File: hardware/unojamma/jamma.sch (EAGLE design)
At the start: 3 parts

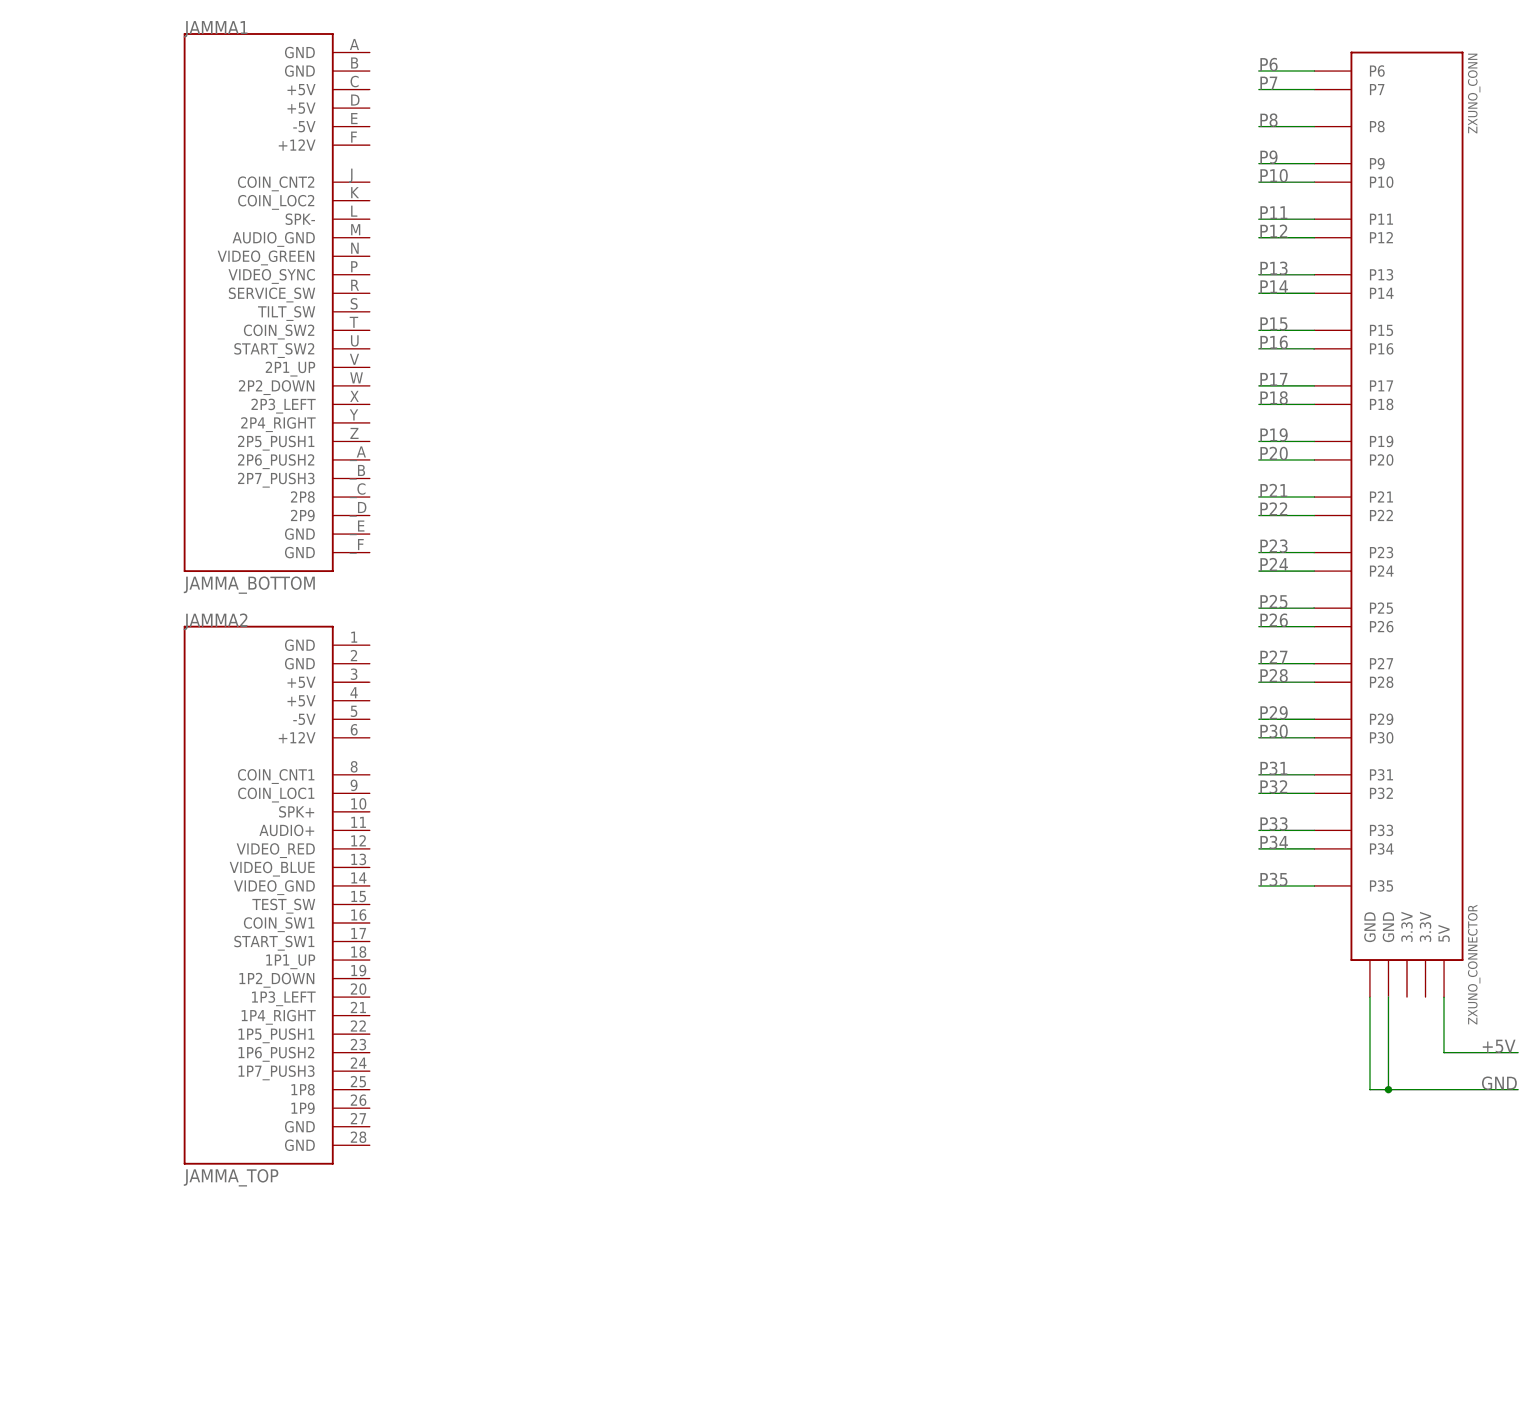
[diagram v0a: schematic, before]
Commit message: Añado conectores y separo placa para que quepa en 10x10cm
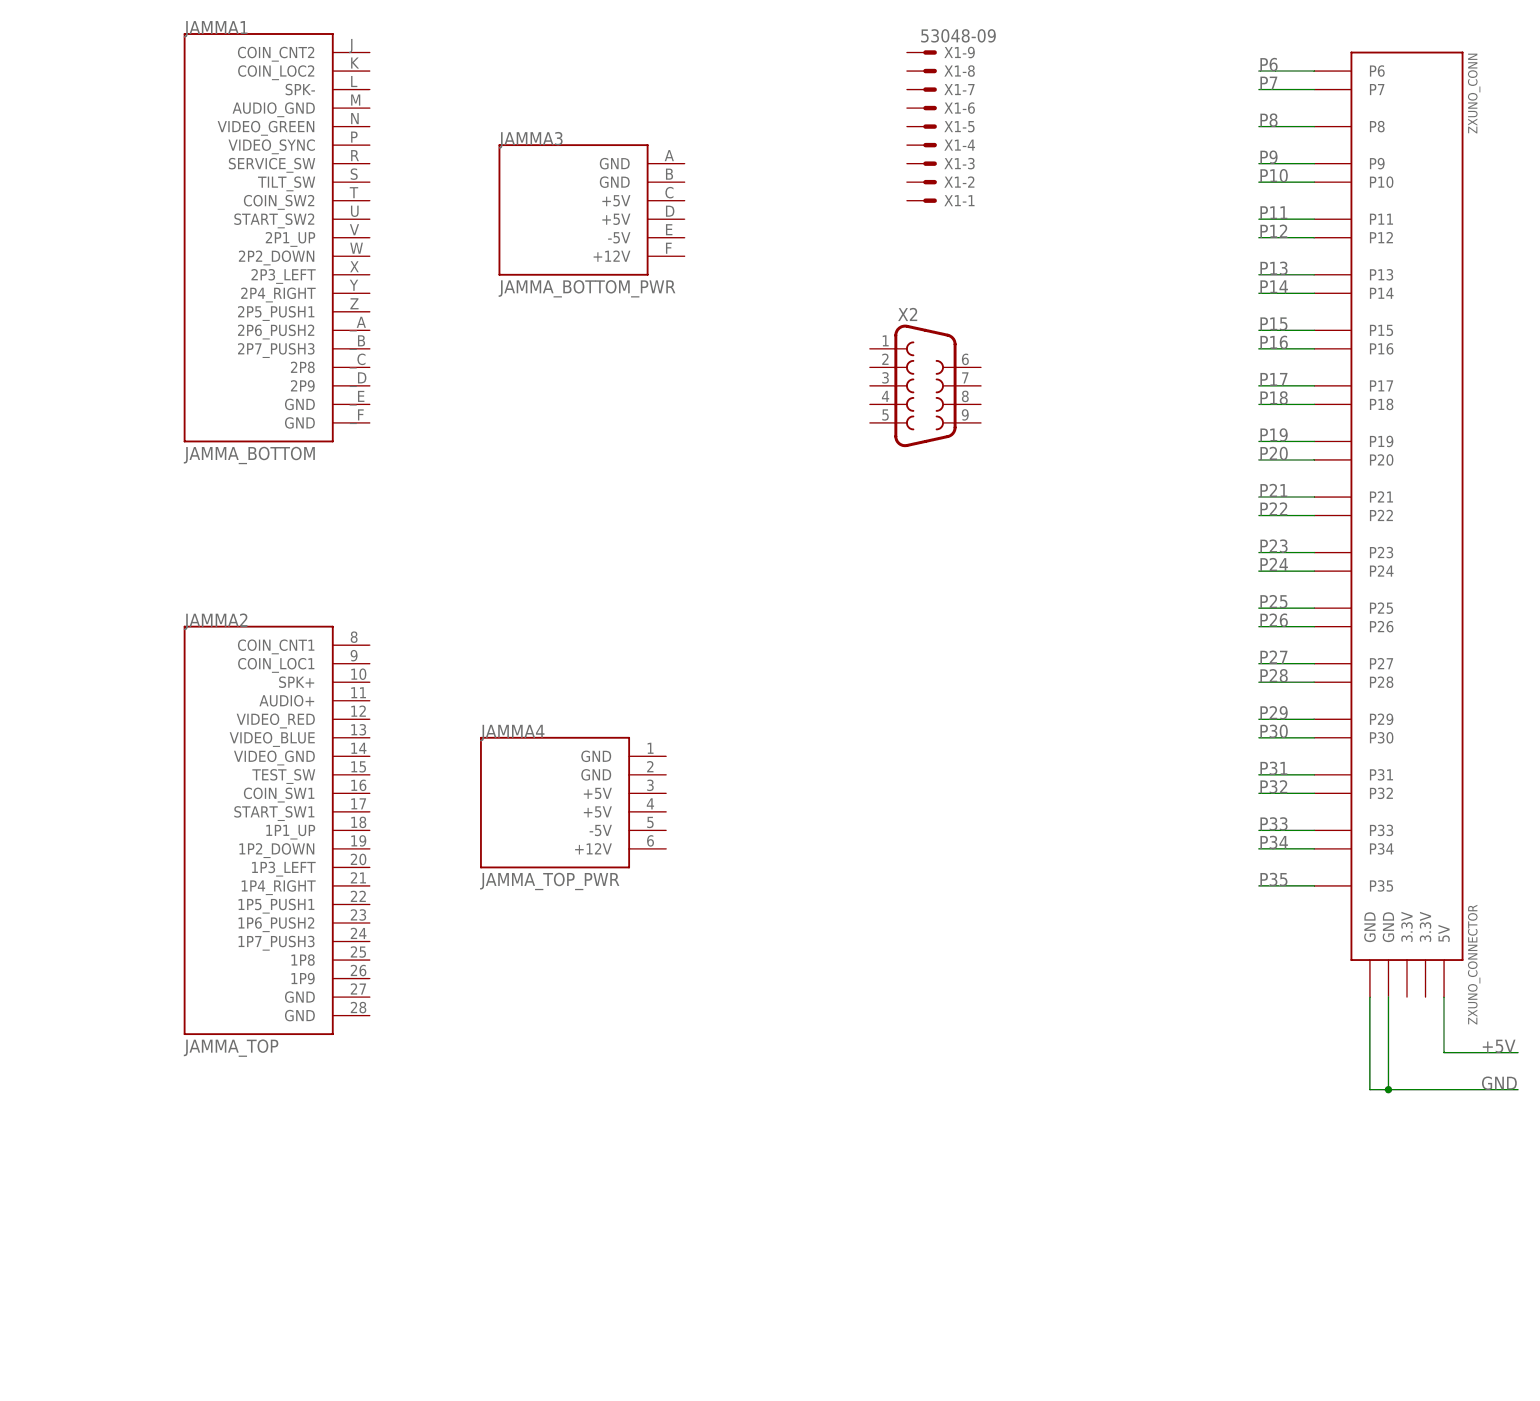
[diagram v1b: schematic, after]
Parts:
- added JAMMA3: JAMMA_BOTTOM_PWR, JAMMA_pwr:JAMMA_BOTTOM_PWR
- added JAMMA4: JAMMA_TOP_PWR, JAMMA_pwr:JAMMA_TOP_PWR
- added X1: 53048-09, con-molex:53048-09
- added X2: (no value), SparkFun-Connectors:DB9MALE
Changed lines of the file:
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@@
 <layer number="54" name="bGND_GNDA" color="7" fill="1" visible="no" active="no"/>
 <layer number="56" name="wert" color="7" fill="1" visible="no" active="no"/>
+<layer number="57" name="tCAD" color="7" fill="1" visible="no" active="no"/>
 <layer number="90" name="Modules" color="5" fill="1" visible="yes" active="yes"/>
 <layer number="91" name="Nets" color="2" fill="1" visible="yes" active="yes"/>
@@
 <layer number="97" name="Info" color="7" fill="1" visible="yes" active="yes"/>
 <layer number="98" name="Guide" color="6" fill="1" visible="yes" active="yes"/>
+<layer number="99" name="SpiceOrder" color="7" fill="1" visible="yes" active="yes"/>
 <layer number="100" name="Muster" color="7" fill="1" visible="yes" active="yes"/>
 <layer number="101" name="Patch_Top" color="7" fill="1" visible="yes" active="yes"/>
@@
 <layer number="111" name="LPC17xx" color="7" fill="1" visible="yes" active="yes"/>
 <layer number="112" name="tSilk" color="7" fill="1" visible="yes" active="yes"/>
+<layer number="113" name="IDFDebug" color="7" fill="1" visible="yes" active="yes"/>
 <layer number="116" name="Patch_BOT" color="7" fill="1" visible="yes" active="yes"/>
+<layer number="118" name="Rect_Pads" color="7" fill="1" visible="yes" active="yes"/>
 <layer number="121" name="_tsilk" color="7" fill="1" visible="yes" active="yes"/>
 <layer number="122" name="_bsilk" color="7" fill="1" visible="yes" active="yes"/>
@@
 <layer number="127" name="_tValues" color="7" fill="1" visible="yes" active="yes"/>
 <layer number="128" name="_bValues" color="7" fill="1" visible="yes" active="yes"/>
+<layer number="130" name="tSilk" color="7" fill="1" visible="yes" active="yes"/>
 <layer number="131" name="prix" color="7" fill="1" visible="yes" active="yes"/>
 <layer number="132" name="test" color="7" fill="1" visible="yes" active="yes"/>
+<layer number="133" name="Ports" color="7" fill="1" visible="yes" active="yes"/>
+<layer number="134" name="Port2" color="7" fill="1" visible="yes" active="yes"/>
+<layer number="135" name="Port3" color="7" fill="1" visible="yes" active="yes"/>
 <layer number="144" name="Drill_legend" color="7" fill="1" visible="yes" active="yes"/>
+<layer number="150" name="Notes" color="7" fill="1" visible="yes" active="yes"/>
 <layer number="151" name="HeatSink" color="7" fill="1" visible="yes" active="yes"/>
 <layer number="152" name="_bDocu" color="7" fill="1" visible="yes" active="yes"/>
+<layer number="153" name="FabDoc1" color="7" fill="1" visible="yes" active="yes"/>
+<layer number="154" name="FabDoc2" color="7" fill="1" visible="yes" active="yes"/>
+<layer number="155" name="FabDoc3" color="7" fill="1" visible="yes" active="yes"/>
 <layer number="199" name="Contour" color="7" fill="1" visible="yes" active="yes"/>
 <layer number="200" name="200bmp" color="7" fill="1" visible="yes" active="yes"/>
@@
 <layer number="223" name="223bmp" color="7" fill="1" visible="yes" active="yes"/>
 <layer number="224" name="224bmp" color="7" fill="1" visible="yes" active="yes"/>
+<layer number="231" name="Eagle3D_PG1" color="7" fill="1" visible="yes" active="yes"/>
+<layer number="232" name="Eagle3D_PG2" color="7" fill="1" visible="yes" active="yes"/>
+<layer number="233" name="Eagle3D_PG3" color="7" fill="1" visible="yes" active="yes"/>
 <layer number="248" name="Housing" color="7" fill="1" visible="yes" active="yes"/>
 <layer number="249" name="Edge" color="7" fill="1" visible="yes" active="yes"/>
@@
 <part name="JAMMA1" library="JAMMA" deviceset="JAMMA_BOTTOM" device=""/>
 <part name="JAMMA2" library="JAMMA" deviceset="JAMMA_TOP" device=""/>
+<part name="JAMMA3" library="JAMMA_pwr" deviceset="JAMMA_BOTTOM_PWR" device=""/>
+<part name="JAMMA4" library="JAMMA_pwr" deviceset="JAMMA_TOP_PWR" device=""/>
+<part name="X1" library="con-molex" deviceset="53?-09" device="048"/>
+<part name="X2" library="SparkFun-Connectors" deviceset="DB9" device="MALE"/>
 </parts>
 <sheets>
@@
 <instance part="JAMMA1" gate="G$1" x="25.4" y="142.24"/>
 <instance part="JAMMA2" gate="G$1" x="27.94" y="60.96"/>
+<instance part="JAMMA3" gate="G$1" x="68.58" y="149.86"/>
+<instance part="JAMMA4" gate="G$1" x="68.58" y="68.58"/>
+<instance part="X1" gate="-9" x="116.84" y="172.72"/>
+<instance part="X1" gate="-8" x="116.84" y="170.18"/>
+<instance part="X1" gate="-7" x="116.84" y="167.64"/>
+<instance part="X1" gate="-6" x="116.84" y="165.1"/>
+<instance part="X1" gate="-5" x="116.84" y="162.56"/>
+<instance part="X1" gate="-4" x="116.84" y="160.02"/>
+<instance part="X1" gate="-3" x="116.84" y="157.48"/>
+<instance part="X1" gate="-2" x="116.84" y="154.94"/>
+<instance part="X1" gate="-1" x="116.84" y="152.4"/>
+<instance part="X2" gate="G$1" x="116.84" y="127"/>
 </instances>
 <busses>

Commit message: Paso a through hole
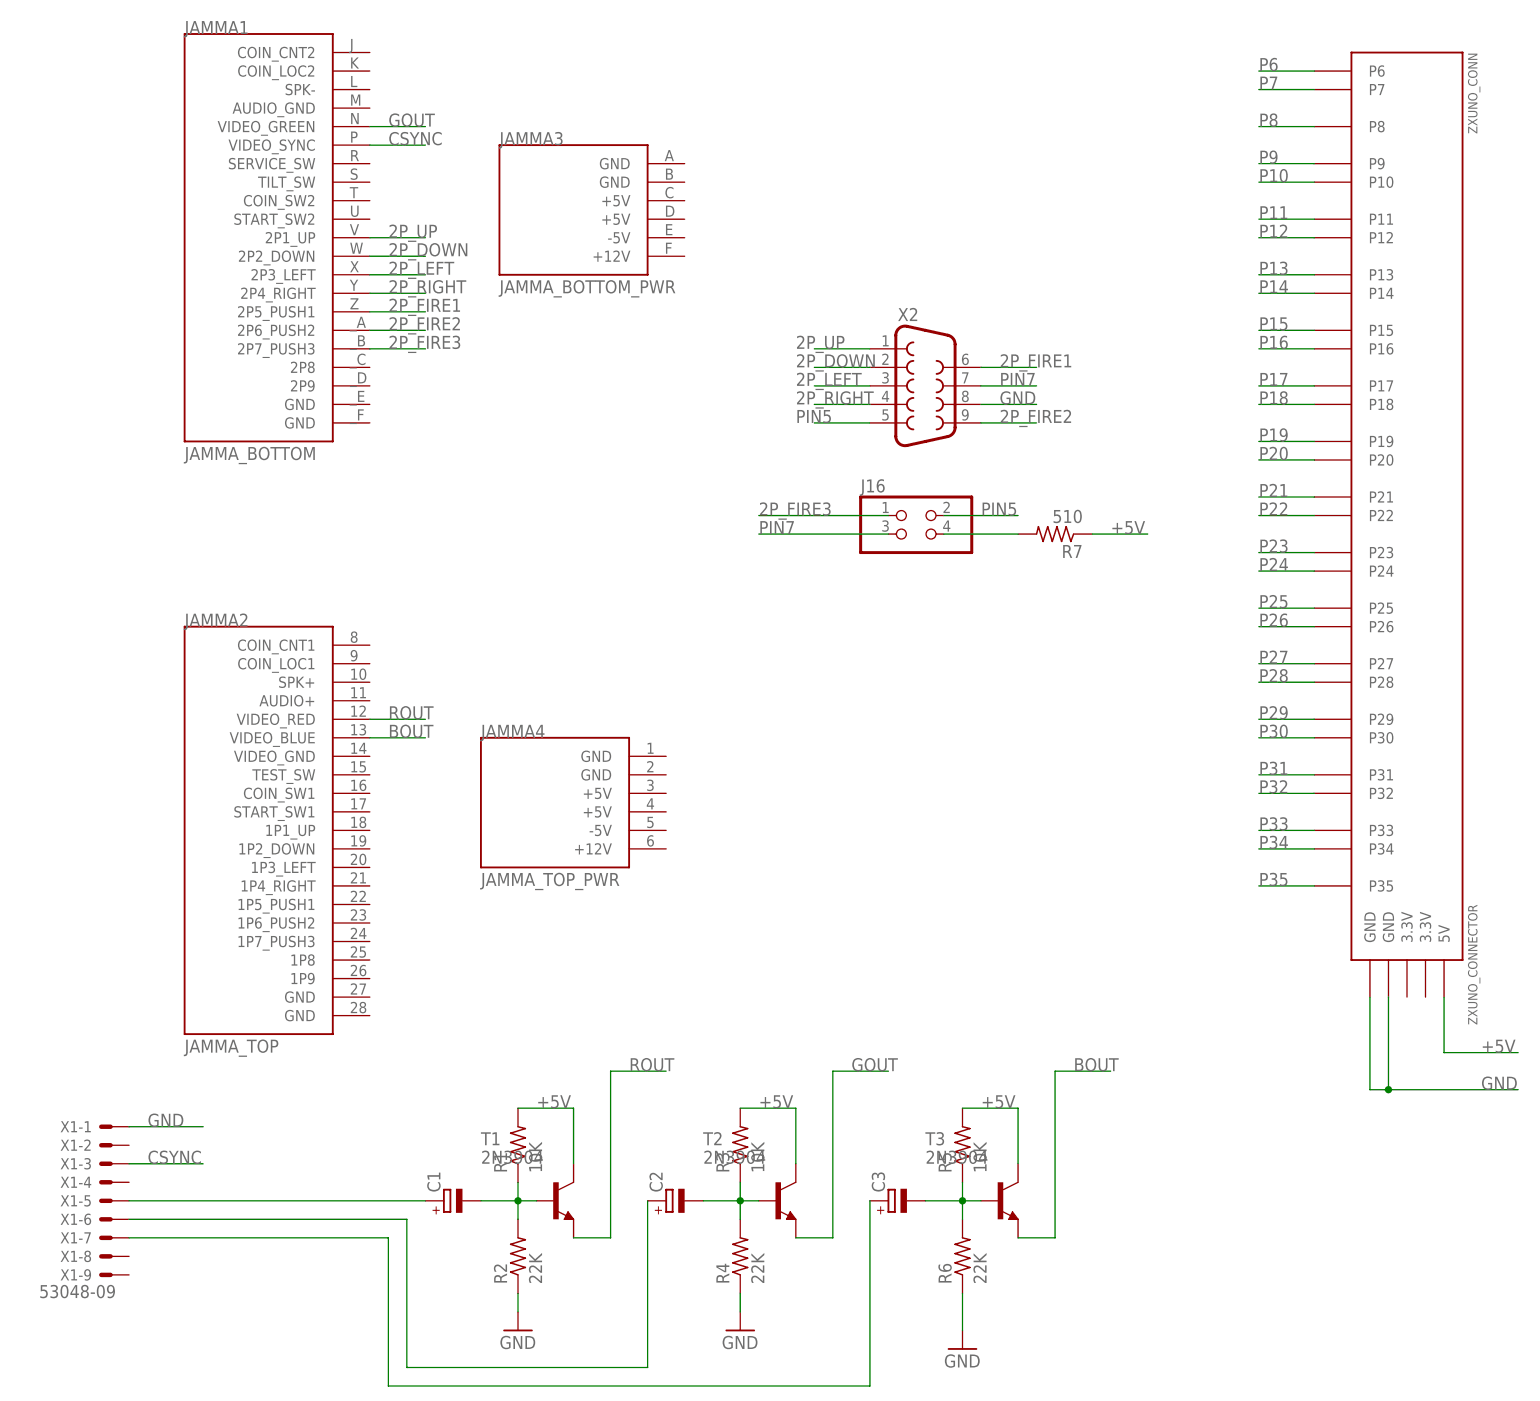
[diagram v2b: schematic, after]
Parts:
- added C1, C2, C3: (no value), rcl:CPOL-EUE2-5
- added J16: (no value), pinhead:PINHD-2X2
- added R1, R3, R5: 10K, adafruit:R-US_0204/7
- added R2, R4, R6: 22K, adafruit:R-US_0204/7
- added R7: 510, rcl:R-US_0204/7
- added T1, T2, T3: 2N3904, transistor:2N3904
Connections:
- new net 2P_DOWN: JAMMA1.2P2_DOWN, X2.2
- new net 2P_FIRE1: JAMMA1.2P5_PUSH1, X2.6
- new net 2P_FIRE2: JAMMA1.2P6_PUSH2, X2.9
- new net 2P_FIRE3: J16.1, JAMMA1.2P7_PUSH3
- new net 2P_LEFT: JAMMA1.2P3_LEFT, X2.3
- new net 2P_RIGHT: JAMMA1.2P4_RIGHT, X2.4
- new net 2P_UP: JAMMA1.2P1_UP, X2.1
- new net BIN: C3.+, X1-7.S
- new net BOUT: JAMMA2.VIDEO_BLUE, T3.E
- new net CSYNC: JAMMA1.VIDEO_SYNC, X1-3.S
- new net GIN: C2.+, X1-6.S
- new net GOUT: JAMMA1.VIDEO_GREEN, T2.E
- new net N$11: C2.-, R3.1, R4.2, T2.B
- new net N$15: J16.4, R7.2
- new net N$4: C1.-, R1.1, R2.2, T1.B
- new net N$8: C3.-, R5.1, R6.2, T3.B
- new net PIN5: J16.2, X2.5
- new net PIN7: J16.3, X2.7
- new net RIN: C1.+, X1-5.S
- new net ROUT: JAMMA2.VIDEO_RED, T1.E
- net +5V: now also R1.2, R3.2, R5.2, R7.1, T1.C, T2.C, T3.C
- net GND: now also R2.1, R4.1, R6.1, X1-1.S, X2.8
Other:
- moved on the sheet: X1-1, X1-2, X1-3, X1-4, X1-5, X1-6, X1-7, X1-8, X1-9
